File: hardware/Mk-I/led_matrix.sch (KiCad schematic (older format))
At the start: 34 parts, among them U9 SSD1306

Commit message: Cleanup schematics
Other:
- note added: "LED matrix"
- note added: "OLED screen"
- note added: "With 24 LEDs we could do a 5x5 (10 GPIOs) matrix, but having the LED logic\nmatrix following the placement layout produces a cleaner PCB. The trade-off is that we\nuse 2 more GPIOs."
- note removed: "With 24 LEDs we could do a 5x5 (10 GPIOs) matrix but having the LED logic matrix \nfollowing the placement layout produces a cleaner PCB. The trade-off is that we\nuse 2 more GPIOs."
- moved on the sheet: D1, D10, D11, D12, D13, D14, D15, D16, D17, D18, D2, D20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

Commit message: HW: Add a DFU mode switch
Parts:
- C25, C26, C27, C28, C29: symbol C -> C-RESCUE-wnm_mk_1
- R15, R7, R8, R9: symbol R -> R-RESCUE-wnm_mk_1
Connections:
- wire segments 56 -> 104
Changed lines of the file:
@@
 EESchema Schematic File Version 2
+LIBS:wnm_mk_1-rescue
 LIBS:power
 LIBS:device
@@
 LIBS:microchip_pic12mcu
 LIBS:microchip_pic16mcu
-LIBS:microchip1
 LIBS:msp430
 LIBS:nxp_armmcu
@@
 LIBS:relays
 LIBS:sensors
-LIBS:special
 LIBS:stm8
 LIBS:stm32
@@
 U 1 1 585D8A6E
 P 2650 2450
+AR Path="/585D8A6E" Ref="D10"  Part="1"
+AR Path="/585D6FEE/585D8A6E" Ref="D10"  Part="1"
 F 0 "D10" H 2650 2550 50  0000 C CNN
 F 1 "LED" H 2650 2350 50  0000 C CNN
@@
 U 1 1 585D8A75
 P 2650 2800
+AR Path="/585D8A75" Ref="D11"  Part="1"
+AR Path="/585D6FEE/585D8A75" Ref="D11"  Part="1"
 F 0 "D11" H 2650 2900 50  0000 C CNN
 F 1 "LED" H 2650 2700 50  0000 C CNN
@@
 U 1 1 585D8A7C
 P 2650 3150
+AR Path="/585D8A7C" Ref="D12"  Part="1"
+AR Path="/585D6FEE/585D8A7C" Ref="D12"  Part="1"
 F 0 "D12" H 2650 3250 50  0000 C CNN
 F 1 "LED" H 2650 3050 50  0000 C CNN
@@
 U 1 1 585D8A83
 P 2650 3500
+AR Path="/585D8A83" Ref="D13"  Part="1"
+AR Path="/585D6FEE/585D8A83" Ref="D13"  Part="1"
 F 0 "D13" H 2650 3600 50  0000 C CNN
 F 1 "LED" H 2650 3400 50  0000 C CNN
@@
 U 1 1 585D8A8A
 P 2650 3850
+AR Path="/585D8A8A" Ref="D14"  Part="1"
+AR Path="/585D6FEE/585D8A8A" Ref="D14"  Part="1"
 F 0 "D14" H 2650 3950 50  0000 C CNN
 F 1 "LED" H 2650 3750 50  0000 C CNN
@@
 U 1 1 585D8A91
 P 2000 2450
+AR Path="/585D8A91" Ref="D1"  Part="1"
+AR Path="/585D6FEE/585D8A91" Ref="D1"  Part="1"
 F 0 "D1" H 2000 2550 50  0000 C CNN
 F 1 "LED" H 2000 2350 50  0000 C CNN
@@
 U 1 1 585D8A98
 P 2000 2800
+AR Path="/585D8A98" Ref="D2"  Part="1"
+AR Path="/585D6FEE/585D8A98" Ref="D2"  Part="1"
 F 0 "D2" H 2000 2900 50  0000 C CNN
 F 1 "LED" H 2000 2700 50  0000 C CNN
@@
 U 1 1 585D8A9F
 P 2000 3150
+AR Path="/585D8A9F" Ref="D3"  Part="1"
+AR Path="/585D6FEE/585D8A9F" Ref="D3"  Part="1"
 F 0 "D3" H 2000 3250 50  0000 C CNN
 F 1 "LED" H 2000 3050 50  0000 C CNN
@@
 U 1 1 585D8AA6
 P 2000 3500
+AR Path="/585D8AA6" Ref="D4"  Part="1"
+AR Path="/585D6FEE/585D8AA6" Ref="D4"  Part="1"
 F 0 "D4" H 2000 3600 50  0000 C CNN
 F 1 "LED" H 2000 3400 50  0000 C CNN
@@
 U 1 1 585D8AAD
 P 2000 3850
+AR Path="/585D8AAD" Ref="D5"  Part="1"
+AR Path="/585D6FEE/585D8AAD" Ref="D5"  Part="1"
 F 0 "D5" H 2000 3950 50  0000 C CNN
 F 1 "LED" H 2000 3750 50  0000 C CNN
@@
 U 1 1 585D8AB4
 P 2000 4200
+AR Path="/585D8AB4" Ref="D6"  Part="1"
+AR Path="/585D6FEE/585D8AB4" Ref="D6"  Part="1"
 F 0 "D6" H 2000 4300 50  0000 C CNN
 F 1 "LED" H 2000 4100 50  0000 C CNN
@@
 U 1 1 585D8ABB
 P 2000 4550
+AR Path="/585D8ABB" Ref="D7"  Part="1"
+AR Path="/585D6FEE/585D8ABB" Ref="D7"  Part="1"
 F 0 "D7" H 2000 4650 50  0000 C CNN
 F 1 "LED" H 2000 4450 50  0000 C CNN
@@
 U 1 1 585D8AC2
 P 2000 4900
+AR Path="/585D8AC2" Ref="D8"  Part="1"
+AR Path="/585D6FEE/585D8AC2" Ref="D8"  Part="1"
 F 0 "D8" H 2000 5000 50  0000 C CNN
 F 1 "LED" H 2000 4800 50  0000 C CNN
@@
 U 1 1 585D8AC9
 P 2000 5250
+AR Path="/585D8AC9" Ref="D9"  Part="1"
+AR Path="/585D6FEE/585D8AC9" Ref="D9"  Part="1"
 F 0 "D9" H 2000 5350 50  0000 C CNN
 F 1 "LED" H 2000 5150 50  0000 C CNN
@@
 U 1 1 585D8AD0
 P 3300 5250
+AR Path="/585D8AD0" Ref="D25"  Part="1"
+AR Path="/585D6FEE/585D8AD0" Ref="D25"  Part="1"
 F 0 "D25" H 3300 5350 50  0000 C CNN
 F 1 "LED" H 3300 5150 50  0000 C CNN
@@
 U 1 1 585D8ADE
 P 3300 3500
+AR Path="/585D8ADE" Ref="D20"  Part="1"
+AR Path="/585D6FEE/585D8ADE" Ref="D20"  Part="1"
 F 0 "D20" H 3300 3600 50  0000 C CNN
 F 1 "LED" H 3300 3400 50  0000 C CNN
@@
 U 1 1 585D8AE5
 P 3300 3850
+AR Path="/585D8AE5" Ref="D21"  Part="1"
+AR Path="/585D6FEE/585D8AE5" Ref="D21"  Part="1"
 F 0 "D21" H 3300 3950 50  0000 C CNN
 F 1 "LED" H 3300 3750 50  0000 C CNN
@@
 U 1 1 585D8AEC
 P 3300 4200
+AR Path="/585D8AEC" Ref="D22"  Part="1"
+AR Path="/585D6FEE/585D8AEC" Ref="D22"  Part="1"
 F 0 "D22" H 3300 4300 50  0000 C CNN
 F 1 "LED" H 3300 4100 50  0000 C CNN
@@
 U 1 1 585D8AF3
 P 3300 4550
+AR Path="/585D8AF3" Ref="D23"  Part="1"
+AR Path="/585D6FEE/585D8AF3" Ref="D23"  Part="1"
 F 0 "D23" H 3300 4650 50  0000 C CNN
 F 1 "LED" H 3300 4450 50  0000 C CNN
@@
 U 1 1 585D8AFA
 P 2650 4200
+AR Path="/585D8AFA" Ref="D15"  Part="1"
+AR Path="/585D6FEE/585D8AFA" Ref="D15"  Part="1"
 F 0 "D15" H 2650 4300 50  0000 C CNN
 F 1 "LED" H 2650 4100 50  0000 C CNN
@@
 U 1 1 585D8B01
 P 2650 4550
+AR Path="/585D8B01" Ref="D16"  Part="1"
+AR Path="/585D6FEE/585D8B01" Ref="D16"  Part="1"
 F 0 "D16" H 2650 4650 50  0000 C CNN
 F 1 "LED" H 2650 4450 50  0000 C CNN
@@
 U 1 1 585D8B08
 P 2650 4900
+AR Path="/585D8B08" Ref="D17"  Part="1"
+AR Path="/585D6FEE/585D8B08" Ref="D17"  Part="1"
 F 0 "D17" H 2650 5000 50  0000 C CNN
 F 1 "LED" H 2650 4800 50  0000 C CNN
@@
 U 1 1 585D8B0F
 P 2650 5250
+AR Path="/585D8B0F" Ref="D18"  Part="1"
+AR Path="/585D6FEE/585D8B0F" Ref="D18"  Part="1"
 F 0 "D18" H 2650 5350 50  0000 C CNN
 F 1 "LED" H 2650 5150 50  0000 C CNN
@@
 U 1 1 585D8B16
 P 3300 4900
+AR Path="/585D8B16" Ref="D24"  Part="1"
+AR Path="/585D6FEE/585D8B16" Ref="D24"  Part="1"
 F 0 "D24" H 3300 5000 50  0000 C CNN
 F 1 "LED" H 3300 4800 50  0000 C CNN
@@
 With 24 LEDs we could do a 5x5 (10 GPIOs) matrix, but having the LED logic\nmatrix following the placement layout produces a cleaner PCB. The trade-off is that we\nuse 2 more GPIOs.
 $Comp
-L R R7
+L R-RESCUE-wnm_mk_1 R7
 U 1 1 5862A3A6
 P 2200 1900
+AR Path="/5862A3A6" Ref="R7"  Part="1"
+AR Path="/585D6FEE/5862A3A6" Ref="R7"  Part="1"
 F 0 "R7" V 2280 1900 40  0000 C CNN
 F 1 "R" V 2207 1901 40  0000 C CNN
@@
 $EndComp
 $Comp
-L R R8
+L R-RESCUE-wnm_mk_1 R8
 U 1 1 5862A65F
 P 2850 1900
+AR Path="/5862A65F" Ref="R8"  Part="1"
+AR Path="/585D6FEE/5862A65F" Ref="R8"  Part="1"
 F 0 "R8" V 2930 1900 40  0000 C CNN
 F 1 "R" V 2857 1901 40  0000 C CNN
@@
 $EndComp
 $Comp
-L R R9
+L R-RESCUE-wnm_mk_1 R9
 U 1 1 5862A6DA
 P 3500 1900
+AR Path="/5862A6DA" Ref="R9"  Part="1"
+AR Path="/585D6FEE/5862A6DA" Ref="R9"  Part="1"
 F 0 "R9" V 3580 1900 40  0000 C CNN
 F 1 "R" V 3507 1901 40  0000 C CNN
@@
 $EndComp
 $Comp
-L C C28
+L C-RESCUE-wnm_mk_1 C28
 U 1 1 586433AA
 P 8525 2225
+AR Path="/586433AA" Ref="C28"  Part="1"
+AR Path="/585D6FEE/586433AA" Ref="C28"  Part="1"
 F 0 "C28" V 8575 2300 40  0000 L CNN
 F 1 "1uF" V 8575 2075 40  0000 L CNN
@@
 $EndComp
 $Comp
-L C C29
+L C-RESCUE-wnm_mk_1 C29
 U 1 1 58643880
 P 8525 2625
+AR Path="/58643880" Ref="C29"  Part="1"
+AR Path="/585D6FEE/58643880" Ref="C29"  Part="1"
 F 0 "C29" V 8575 2700 40  0000 L CNN
 F 1 "1uF" V 8575 2475 40  0000 L CNN
@@
 	6975 3425 6975 5150
 $Comp
-L C C25
+L C-RESCUE-wnm_mk_1 C25
 U 1 1 586463AC
 P 7425 3625
+AR Path="/586463AC" Ref="C25"  Part="1"
+AR Path="/585D6FEE/586463AC" Ref="C25"  Part="1"
 F 0 "C25" V 7475 3700 40  0000 L CNN
 F 1 "10uF" V 7475 3475 40  0000 L CNN
@@
 Connection ~ 6975 3625
 $Comp
-L GND #PWR031
+L GND-RESCUE-wnm_mk_1 #PWR031
 U 1 1 586468A3
 P 6975 5150
+AR Path="/586468A3" Ref="#PWR031"  Part="1"
+AR Path="/585D6FEE/586468A3" Ref="#PWR031"  Part="1"
 F 0 "#PWR031" H 6975 5150 30  0001 C CNN
 F 1 "GND" H 6975 5080 30  0001 C CNN
@@
 $EndComp
 $Comp
-L R R15
+L R-RESCUE-wnm_mk_1 R15
 U 1 1 58646E77
 P 7800 4425
+AR Path="/58646E77" Ref="R15"  Part="1"
+AR Path="/585D6FEE/58646E77" Ref="R15"  Part="1"
 F 0 "R15" V 7880 4425 40  0000 C CNN
 F 1 "R" V 7807 4426 40  0000 C CNN
@@
 $EndComp
 $Comp
-L C C26
+L C-RESCUE-wnm_mk_1 C26
 U 1 1 58646F61
 P 7800 4625
+AR Path="/58646F61" Ref="C26"  Part="1"
+AR Path="/585D6FEE/58646F61" Ref="C26"  Part="1"
 F 0 "C26" V 7850 4700 40  0000 L CNN
 F 1 "10uF" V 7850 4475 40  0000 L CNN
@@
 $EndComp
 $Comp
-L C C27
+L C-RESCUE-wnm_mk_1 C27
 U 1 1 58647031
 P 7800 4825
+AR Path="/58647031" Ref="C27"  Part="1"
+AR Path="/585D6FEE/58647031" Ref="C27"  Part="1"
 F 0 "C27" V 7850 4900 40  0000 L CNN
 F 1 "10uF" V 7850 4675 40  0000 L CNN
@@
 Text Notes 7050 1100 0    315  ~ 0
 OLED screen
+Wire Wire Line
+	3100 5250 3150 5250
+Wire Wire Line
+	3500 5250 3450 5250
+Wire Wire Line
+	3500 4900 3450 4900
+Wire Wire Line
+	3100 4900 3150 4900
+Wire Wire Line
+	3100 4550 3150 4550
+Wire Wire Line
+	3450 4550 3500 4550
+Wire Wire Line
+	3500 4200 3450 4200
+Wire Wire Line
+	3100 4200 3150 4200
+Wire Wire Line
+	3100 3850 3150 3850
+Wire Wire Line
+	3450 3850 3500 3850
+Wire Wire Line
+	3500 3500 3450 3500
+Wire Wire Line
+	3150 3500 3100 3500
+Wire Wire Line
+	2850 2450 2800 2450
+Wire Wire Line
+	2450 2450 2500 2450
+Wire Wire Line
+	2450 2800 2500 2800
+Wire Wire Line
+	2800 2800 2850 2800
+Wire Wire Line
+	2200 2450 2150 2450
+Wire Wire Line
+	1800 2450 1850 2450
+Wire Wire Line
+	1800 2800 1850 2800
+Wire Wire Line
+	1800 3150 1850 3150
+Wire Wire Line
+	2150 2800 2200 2800
+Wire Wire Line
+	2150 3150 2200 3150
+Wire Wire Line
+	2450 3150 2500 3150
+Wire Wire Line
+	2800 3150 2850 3150
+Wire Wire Line
+	2850 3500 2800 3500
+Wire Wire Line
+	2450 3500 2500 3500
+Wire Wire Line
+	2200 3500 2150 3500
+Wire Wire Line
+	1800 3500 1850 3500
+Wire Wire Line
+	1800 3850 1850 3850
+Wire Wire Line
+	2150 3850 2200 3850
+Wire Wire Line
+	2450 3850 2500 3850
+Wire Wire Line
+	2800 3850 2850 3850
+Wire Wire Line
+	2850 4200 2800 4200
+Wire Wire Line
+	2450 4200 2500 4200
+Wire Wire Line
+	2200 4200 2150 4200
+Wire Wire Line
+	1800 4200 1850 4200
+Wire Wire Line
+	1850 4550 1800 4550
+Wire Wire Line
+	2150 4550 2200 4550
+Wire Wire Line
+	2450 4550 2500 4550
+Wire Wire Line
+	2800 4550 2850 4550
+Wire Wire Line
+	2850 4900 2800 4900
+Wire Wire Line
+	2450 4900 2500 4900
+Wire Wire Line
+	2150 4900 2200 4900
+Wire Wire Line
+	1850 4900 1800 4900
+Wire Wire Line
+	1850 5250 1800 5250
+Wire Wire Line
+	2200 5250 2150 5250
+Wire Wire Line
+	2450 5250 2500 5250
+Wire Wire Line
+	2850 5250 2800 5250
 $EndSCHEMATC

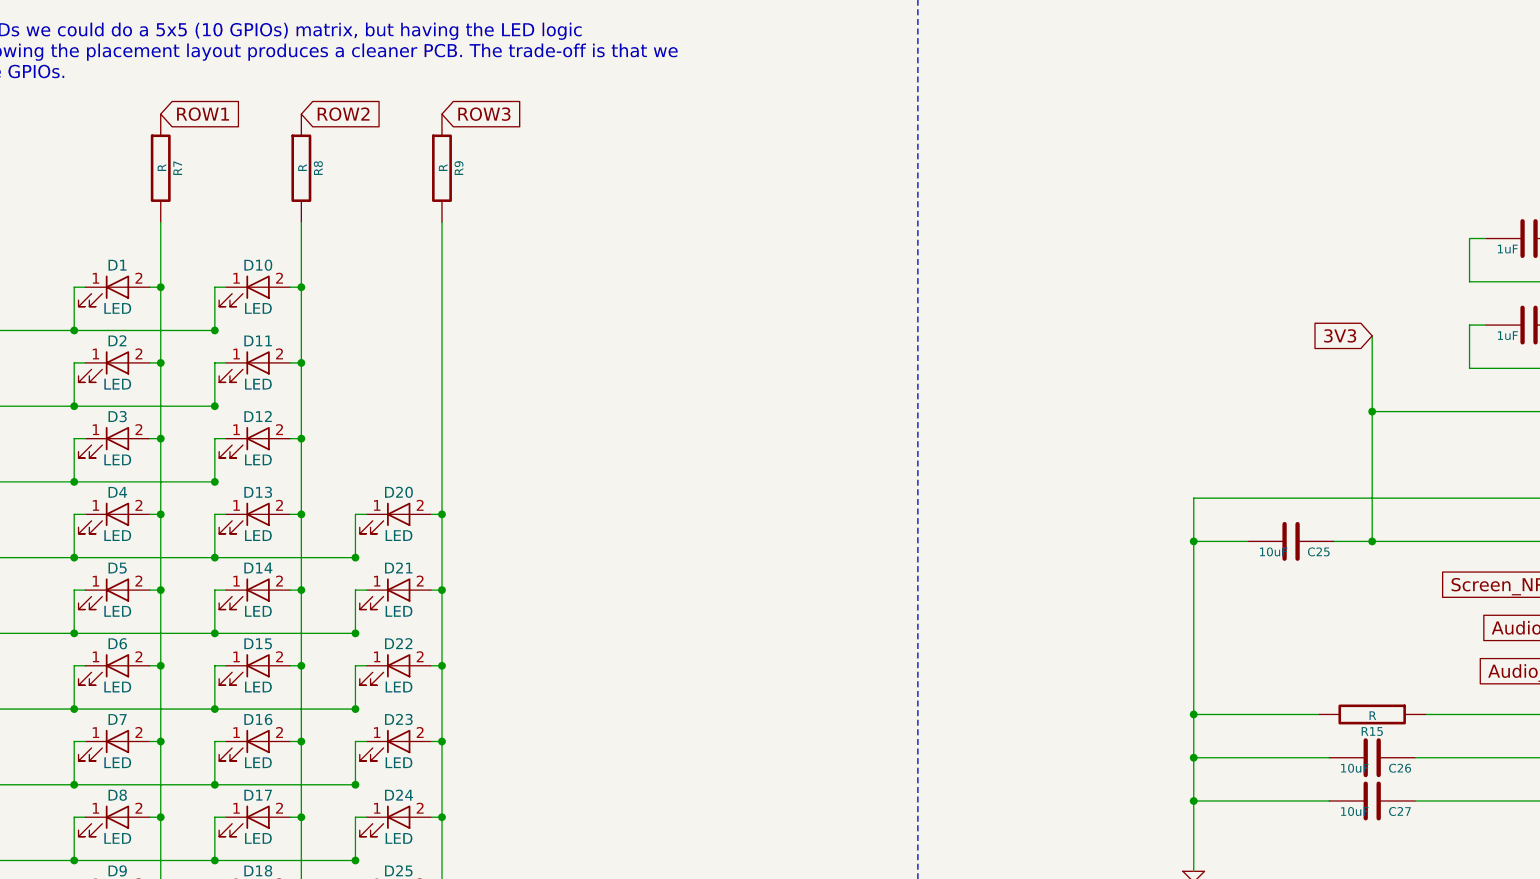
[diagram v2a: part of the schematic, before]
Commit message: HW: Start Mk-I rev-A known problems
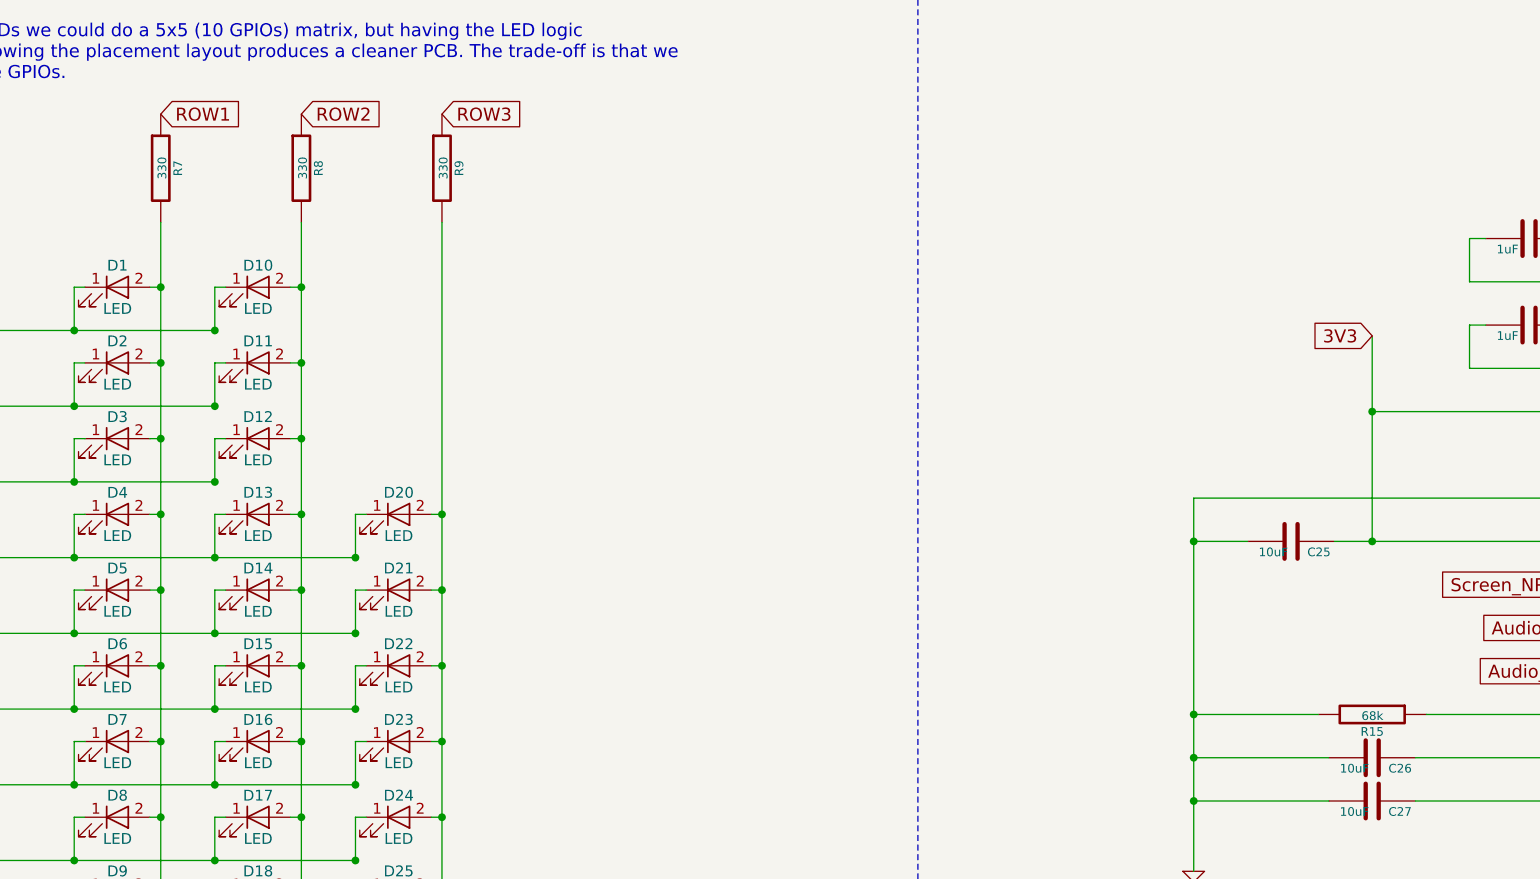
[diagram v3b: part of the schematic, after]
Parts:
- R15: value R -> 68k
- R7, R8, R9: value R -> 330
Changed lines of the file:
@@
 AR Path="/585D6FEE/5862A3A6" Ref="R7"  Part="1"
 F 0 "R7" V 2280 1900 40  0000 C CNN
-F 1 "R" V 2207 1901 40  0000 C CNN
+F 1 "330" V 2207 1901 40  0000 C CNN
 F 2 "Resistors_SMD:R_0805" V 2130 1900 30  0001 C CNN
 F 3 "" H 2200 1900 30  0000 C CNN
@@
 AR Path="/585D6FEE/5862A65F" Ref="R8"  Part="1"
 F 0 "R8" V 2930 1900 40  0000 C CNN
-F 1 "R" V 2857 1901 40  0000 C CNN
+F 1 "330" V 2857 1901 40  0000 C CNN
 F 2 "Resistors_SMD:R_0805" V 2780 1900 30  0001 C CNN
 F 3 "" H 2850 1900 30  0000 C CNN
@@
 AR Path="/585D6FEE/5862A6DA" Ref="R9"  Part="1"
 F 0 "R9" V 3580 1900 40  0000 C CNN
-F 1 "R" V 3507 1901 40  0000 C CNN
+F 1 "330" V 3507 1901 40  0000 C CNN
 F 2 "Resistors_SMD:R_0805" V 3430 1900 30  0001 C CNN
 F 3 "" H 3500 1900 30  0000 C CNN
@@
 AR Path="/585D6FEE/58646E77" Ref="R15"  Part="1"
 F 0 "R15" V 7880 4425 40  0000 C CNN
-F 1 "R" V 7807 4426 40  0000 C CNN
+F 1 "68k" V 7807 4426 40  0000 C CNN
 F 2 "Resistors_SMD:R_0805" V 7730 4425 30  0001 C CNN
 F 3 "" H 7800 4425 30  0000 C CNN
